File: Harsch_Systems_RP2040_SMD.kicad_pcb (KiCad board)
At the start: 2 copper layers, 140 parts, among them J1 Jack-DC, J2 USB_A, J3 DEBUG, J4 Conn_01x08_Female, J5 Conn_01x08_Female, J6 Conn_01x04_Female, J7 Conn_01x06_Female, Q1 BSS123, Q2 BSS123, Q3 BSS123, Q4 BSS123, Q5 BCP56, Q6 BCP56, Q7 BCP56, Q8 BCP56, SW1 SW_MEC_5E, U1 RP2040, U2 W25Q32JVSSIQ_TR, U3 LM324, U4 PC847, U5 LM324, U6 PC847, U7 PC847, U8 LM324, Y1 12MHz

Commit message: Finished the schematic, except for maybe a couple test points.
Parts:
- removed D1: D, Diode_SMD:D_0805_2012Metric
- added C35: 2.2μ, Capacitor_SMD:C_0805_2012Metric, F.Cu at (219.1, 135.9)
- added C36: 2.2μ, Capacitor_SMD:C_0805_2012Metric, F.Cu at (209.1, 121.2)
- added C37: 2.2μ, Capacitor_SMD:C_0805_2012Metric, F.Cu at (213.6, 118.2)
- added C38: 2.2μ, Capacitor_SMD:C_0805_2012Metric, F.Cu at (218.0, 112.1)
- added C39: 2.2μ, Capacitor_SMD:C_0805_2012Metric, F.Cu at (209.1, 118.2)
- added C40: 2.2μ, Capacitor_SMD:C_0805_2012Metric, F.Cu at (213.6, 115.2)
- added C41: 2.2μ, Capacitor_SMD:C_0805_2012Metric, F.Cu at (209.1, 115.2)
- added C42: 2.2μ, Capacitor_SMD:C_0805_2012Metric, F.Cu at (213.6, 112.1)
- added C43: 2.2μ, Capacitor_SMD:C_0805_2012Metric, F.Cu at (209.1, 112.1)
- added D3: D, Diode_SMD:D_0805_2012Metric, F.Cu at (238.2, 112.2)
- added D4: D, Diode_SMD:D_0805_2012Metric, F.Cu at (242.6, 112.2)
- added J8: DEBUG, Connector_PinHeader_2.54mm:PinHeader_1x03_P2.54mm_Vertical, F.Cu at (154.3, 55.9)
- added L1: 6.8μ, Inductor_SMD:L_Vishay_IHLP-2020, F.Cu at (204.9, 137.7)
- added R78: 10k, Resistor_SMD:R_0805_2012Metric, F.Cu at (209.1, 124.2)
- added R79: 22k, Resistor_SMD:R_0805_2012Metric, F.Cu at (222.4, 112.1)
- added R80: 22k, Resistor_SMD:R_0805_2012Metric, F.Cu at (218.0, 115.1)
- added U10: TLV9304IDR, Package_SO:SOIC-14_3.9x8.7mm_P1.27mm, F.Cu at (119.4, 134.5)
- added U9: ELQ3H7, Package_SO:SOP-16_3.9x9.9mm_P1.27mm, F.Cu at (165.2, 92.7)
- C1, C5: value 0.1μ -> 1μ; footprint Capacitor_SMD:C_0603_1608Metric -> Capacitor_SMD:C_0805_2012Metric
- C10, C11: value 1μ -> 0.1μ; footprint Capacitor_SMD:C_0805_2012Metric -> Capacitor_SMD:C_0603_1608Metric
- C12: value 27p -> 22μ
- C14: value 27p -> 0.1μ; footprint Capacitor_SMD:C_0805_2012Metric -> Capacitor_SMD:C_0603_1608Metric
- C15: value .47μ -> 0.1μ; footprint Capacitor_SMD:C_0805_2012Metric -> Capacitor_SMD:C_0603_1608Metric
- C16: value .47μ -> 22μ
- C17, C18: value 2.2µ -> 0.1μ; footprint Capacitor_SMD:C_0805_2012Metric -> Capacitor_SMD:C_0603_1608Metric
- C19, C20: value 2.2μ -> 1μ
- C21, C23: value 2.2μ -> 27p
- C22: value 2.2μ -> 0.1μ; footprint Capacitor_SMD:C_0805_2012Metric -> Capacitor_SMD:C_0603_1608Metric
- C24, C25: value 2.2μ -> .47μ
- C26, C27: value 2.2μ -> 2.2µ
- C3, C8: value 0.1μ -> 33n; footprint Capacitor_SMD:C_0603_1608Metric -> Capacitor_SMD:C_0805_2012Metric
- C4: value 0.1μ -> 10μ; footprint Capacitor_SMD:C_0603_1608Metric -> Capacitor_SMD:C_0805_2012Metric
- D2: value D -> D_Schottky; footprint Diode_SMD:D_0805_2012Metric -> Diode_SMD:D_SOD-123
- J2: value USB_A -> Conn_01x02_Male; footprint Connector_USB:USB_Micro-B_GCT_USB3076-30-A -> Connector_PinSocket_2.54mm:PinSocket_1x02_P2.54mm_Vertical
- J3: value DEBUG -> Conn_01x08_Female; footprint Connector_PinHeader_2.54mm:PinHeader_1x03_P2.54mm_Vertical -> Connector_PinHeader_2.54mm:PinHeader_1x08_P2.54mm_Vertical
- J5: value Conn_01x08_Female -> Conn_01x04_Female; footprint Connector_PinHeader_2.54mm:PinHeader_1x08_P2.54mm_Vertical -> Connector_PinHeader_2.54mm:PinHeader_1x04_P2.54mm_Vertical
- J6: value Conn_01x04_Female -> Conn_01x06_Female; footprint Connector_PinHeader_2.54mm:PinHeader_1x04_P2.54mm_Vertical -> Connector_PinHeader_2.54mm:PinHeader_1x06_P2.54mm_Vertical
- J7: value Conn_01x06_Female -> USB_A; footprint Connector_PinHeader_2.54mm:PinHeader_1x06_P2.54mm_Vertical -> Connector_USB:USB_Micro-B_GCT_USB3076-30-A
- Q5, Q6, Q7, Q8: footprint Package_TO_SOT_SMD:SOT-223-3_TabPin2 -> Package_TO_SOT_SMD:SOT-223
- R1, R2: value 27 -> 10K
- R10: value 10k -> 1K
- R11: value 10k -> 22k
- R12, R71, R72: value 2.2k -> 22k
- R13, R70: value 2.2k -> 10k
- R14: value 150 -> 10k
- R15: value 1M -> 2.2k
- R16, R30, R31, R38, R39: value 150 -> 2.2k
- R17: value 1M -> 150
- R18, R20: value 47 -> 1M; footprint Resistor_SMD:R_1210_3225Metric -> Resistor_SMD:R_0805_2012Metric
- R19: value 47 -> 150; footprint Resistor_SMD:R_1210_3225Metric -> Resistor_SMD:R_0805_2012Metric
- R22, R23: value 150 -> 47; footprint Resistor_SMD:R_0805_2012Metric -> Resistor_SMD:R_1210_3225Metric
- R24: value 2.2k -> 47; footprint Resistor_SMD:R_0805_2012Metric -> Resistor_SMD:R_1210_3225Metric
- R25, R26, R34: value 2.2k -> 150
- R3: value 10K -> 10k
- R32, R40: value 10 -> 2.2k
- R33, R41: value 10 -> 150
- R35, R36: value 2.2k -> 10
- R4: value 1K -> 53.6k
- R42: value 2.2k -> 150; footprint Resistor_SMD:R_1210_3225Metric -> Resistor_SMD:R_0805_2012Metric
- R43: value 2.2k -> 10; footprint Resistor_SMD:R_1210_3225Metric -> Resistor_SMD:R_0805_2012Metric
- R44: value 20k -> 10
- R45, R49: value 20k -> 2.2k; footprint Resistor_SMD:R_0805_2012Metric -> Resistor_SMD:R_1210_3225Metric
- R47: value 2.2k -> 20k; footprint Resistor_SMD:R_1210_3225Metric -> Resistor_SMD:R_0805_2012Metric
- R5: value 10K -> 1K
- R50: value 470 -> 2.2k; footprint Resistor_SMD:R_0805_2012Metric -> Resistor_SMD:R_1210_3225Metric
- R51: value 470 -> 20k
- R52: value 2.2k -> 20k
- R53, R59: value 4.7k -> 470
- R54, R60: value 2.2k -> 470
- R55, R61: value 4.7k -> 2.2k
- R56: value 470 -> 4.7k
- R57: value 470 -> 2.2k
- R58, R62, R64: value 2.2k -> 4.7k
- R6: value R_US -> 10K
- R66, R67, R74, R75: value 10k -> 2.2k
- R68, R76: value 22k -> 2.2k
- R69, R77: value 22k -> 10k
- R7: value 1K -> DNP
- R8, R9: value 22k -> 27
- SW1: footprint Button_Switch_SMD:Panasonic_EVQPUJ_EVQPUA -> Button_Switch_SMD:SW_DIP_SPSTx02_Slide_6.7x6.64mm_W6.73mm_P2.54mm_LowProfile_JPin
- U1: value RP2040 -> XC6210B332MR; footprint MCU_RaspberryPi_and_Boards:RP2040-QFN-56 -> Package_TO_SOT_SMD:SOT-23-5
- U2: value W25Q32JVSSIQ_TR -> TPS62933; footprint digikey-footprints:SOIC-8_W5.6mm -> Package_DFN_QFN:Texas_VSON-HR-8_1.5x2mm_P0.5mm
- U3: value LM324 -> RP2040; footprint Package_DIP:DIP-14_W7.62mm -> MCU_RaspberryPi_and_Boards:RP2040-QFN-56
- U4: value PC847 -> W25Q32JVSSIQ_TR; footprint Package_DIP:DIP-16_W7.62mm -> digikey-footprints:SOIC-8_W5.6mm
- U5: value LM324 -> TLV9004xRUCR; footprint Package_DIP:DIP-14_W7.62mm -> Package_SO:SOIC-14_3.9x8.7mm_P1.27mm
- U6: value PC847 -> ELQ3H7; footprint Package_DIP:DIP-16_W7.62mm -> Package_SO:SOP-16_3.9x9.9mm_P1.27mm
- U7: value PC847 -> TLV9004xRUCR; footprint Package_DIP:DIP-16_W7.62mm -> Package_SO:SOIC-14_3.9x8.7mm_P1.27mm
- U8: value LM324 -> ELQ3H7; footprint Package_DIP:DIP-14_W7.62mm -> Package_SO:SOP-16_3.9x9.9mm_P1.27mm
- moved J5 96.7 mm to (184.8, 26.0)
- moved J4 95.0 mm to (175.3, 21.0), turned to 270 degrees
- moved J6 88.2 mm to (184.8, 39.4)
- moved J3 82.0 mm to (150.5, 21.0), turned to 270 degrees
- moved SW1 68.4 mm to (172.1, 31.1)
- moved U3 66.0 mm to (154.9, 36.2)
- moved U8 62.4 mm to (141.0, 107.7)
- moved J7 43.8 mm to (124.5, 32.4), turned to 90 degrees
- moved J1 24.5 mm to (128.3, 50.8)
- moved U6 22.9 mm to (141.0, 92.7)
- moved U5 20.4 mm to (119.4, 121.3)
- moved U7 19.1 mm to (140.5, 121.3)
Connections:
- C1 pad 1: +1V1 -> +5V
- C10 pad 1: +1V1 -> +3V3
- C12 pad 1: /XIN -> +5V
- C14 pad 1: Net-(C14-Pad1) -> +5V
- C15 pad 1: /10V Input/ADC0 -> +3V3
- C16 pad 1: /10V Input/ADC1 -> +5V
- C17 pad 1: /20mA Input/ADC2 -> +3V3
- C18 pad 1: /20mA Input/ADC3 -> +3V3
- C19 pad 1: Net-(C19-Pad1) -> +1V1
- C2 pad 1: +1V1 -> +24V
- C20 pad 1: Net-(C20-Pad1) -> +3V3
- C21 pad 1: Net-(C21-Pad1) -> /XIN
- C22 pad 1: Net-(C22-Pad1) -> +3V3
- C24 pad 1: Net-(C24-Pad1) -> /ADC0
- C25 pad 1: Net-(C25-Pad1) -> /ADC1
- C26 pad 1: Net-(C26-Pad1) -> /ADC2
- C27 pad 1: Net-(C27-Pad1) -> /ADC3
- C3 pad 1: +3V3 -> Net-(C3-Pad1)
- C4 pad 1: +3V3 -> +24V
- C6 pad 1: +3V3 -> +1V1
- C7 pad 1: +3V3 -> +1V1
- C8 pad 1: +3V3 -> Net-(C8-Pad1)
- C8 pad 2: GND -> Net-(C8-Pad2)
- D2 pad 1: /Digital Input/IN+1 -> +24V
- J1 pad 1: Net-(J1-Pad1) -> Net-(D2-Pad2)
- J1 pad 2: Net-(J1-Pad2) -> GND
- J2 pad 1: Net-(J2-Pad1) -> GND
- J3 pad 1: /SWCLK -> /10V Output/OUT0
- J3 pad 2: GND -> /10V Output/OUT1
- J3 pad 3: /SWDIO -> /10V Output/OUT2
- J4 pad 1: Net-(J4-Pad1) -> /Digital Input/IN+0
- J4 pad 2: Net-(J4-Pad2) -> /Digital Input/IN-0
- J4 pad 3: Net-(J4-Pad3) -> /Digital Input/IN+1
- J4 pad 4: Net-(J4-Pad4) -> /Digital Input/IN-1
- J4 pad 5: Net-(J4-Pad5) -> /Digital Input/IN+2
- J4 pad 6: Net-(J4-Pad6) -> /Digital Input/IN-2
- J4 pad 7: Net-(J4-Pad7) -> /Digital Input/IN+3
- J4 pad 8: Net-(J4-Pad8) -> /Digital Input/IN-3
- J5 pad 1: Net-(J5-Pad1) -> /Digital Output/OUT0
- J5 pad 2: Net-(J5-Pad2) -> /Digital Output/OUT1
- J5 pad 3: Net-(J5-Pad3) -> /Digital Output/OUT2
- J5 pad 4: Net-(J5-Pad4) -> /Digital Output/OUT3
- J6 pad 1: Net-(J6-Pad1) -> /10V Input/VIN0
- J6 pad 2: Net-(J6-Pad2) -> /10V Input/VIN1
- J6 pad 3: Net-(J6-Pad3) -> /20mA Input/IN2
- J6 pad 4: Net-(J6-Pad4) -> /20mA Input/OUT2
- J7 pad 4: Net-(J7-Pad4) -> GND
- J7 pad 5: Net-(J7-Pad5) -> GND
- J7 pad 6: Net-(J7-Pad6) -> (no net)
- R1 pad 1: /USB_DP -> Net-(R1-Pad1)
- R1 pad 2: Net-(J2-Pad3) -> +5V
- R10 pad 1: GND -> /XOUT
- R10 pad 2: Net-(R10-Pad2) -> Net-(C23-Pad1)
- R11 pad 1: GND -> Net-(R11-Pad1)
- R11 pad 2: Net-(R11-Pad2) -> /10V Input/VIN0
- R12 pad 1: /10V Input/ADC0 -> Net-(R12-Pad1)
- R12 pad 2: Net-(R12-Pad2) -> /10V Input/VIN1
- R13 pad 1: /10V Input/ADC1 -> GND
- R13 pad 2: Net-(R13-Pad2) -> Net-(R11-Pad1)
- R14 pad 1: Net-(R14-Pad1) -> GND
- R14 pad 2: /20mA Input/IN2 -> Net-(R12-Pad1)
- R15 pad 1: GND -> /ADC0
- R15 pad 2: /20mA Input/OUT2 -> Net-(R15-Pad2)
- R16 pad 1: Net-(R16-Pad1) -> /ADC1
- R16 pad 2: /20mA Input/IN3 -> Net-(R16-Pad2)
- R17 pad 1: GND -> Net-(R17-Pad1)
- R17 pad 2: /20mA Input/OUT3 -> /20mA Input/IN2
- R18 pad 2: Net-(R18-Pad2) -> /20mA Input/OUT2
- R19 pad 1: GND -> Net-(R19-Pad1)
- R19 pad 2: Net-(R19-Pad2) -> /20mA Input/IN3
- R2 pad 1: /USB_DM -> Net-(R2-Pad1)
- R2 pad 2: Net-(J2-Pad2) -> +3V3
- R20 pad 2: Net-(R20-Pad2) -> /20mA Input/OUT3
- R24 pad 1: /20mA Input/ADC2 -> GND
- R24 pad 2: Net-(R22-Pad2) -> Net-(R24-Pad2)
- R25 pad 1: /20mA Input/ADC3 -> GND
- R25 pad 2: Net-(R23-Pad2) -> Net-(R25-Pad2)
- R26 pad 1: Net-(C19-Pad1) -> GND
- R26 pad 2: /20mA Output/PWM4 -> Net-(R26-Pad2)
- R27 pad 1: Net-(C20-Pad1) -> /ADC2
- R27 pad 2: /20mA Output/PWM5 -> Net-(R25-Pad2)
- R28 pad 1: Net-(C21-Pad1) -> /ADC3
- R28 pad 2: Net-(C19-Pad1) -> Net-(R26-Pad2)
- R29 pad 1: Net-(C22-Pad1) -> Net-(C28-Pad1)
- R29 pad 2: Net-(C20-Pad1) -> /PWM4
- R3 pad 1: Net-(R3-Pad1) -> GND
- R3 pad 2: +3V3 -> Net-(R3-Pad2)
- R30 pad 1: Net-(Q1-Pad2) -> Net-(C29-Pad1)
- R30 pad 2: GND -> /PWM5
- R31 pad 1: Net-(Q2-Pad2) -> Net-(C30-Pad1)
- R31 pad 2: GND -> Net-(C28-Pad1)
- R32 pad 1: Net-(Q1-Pad1) -> Net-(C31-Pad1)
- R32 pad 2: Net-(R32-Pad2) -> Net-(C29-Pad1)
- R33 pad 1: Net-(Q2-Pad1) -> Net-(Q1-Pad2)
- R33 pad 2: Net-(R33-Pad2) -> GND
- R34 pad 1: Net-(C23-Pad1) -> Net-(Q2-Pad2)
- R34 pad 2: /20mA Output/PWM6 -> GND
- R35 pad 1: Net-(C24-Pad1) -> Net-(Q1-Pad1)
- R35 pad 2: /20mA Output/PWM7 -> Net-(R35-Pad2)
- R36 pad 1: Net-(C25-Pad1) -> Net-(Q2-Pad1)
- R36 pad 2: Net-(C23-Pad1) -> Net-(R36-Pad2)
- R37 pad 1: Net-(C26-Pad1) -> Net-(C32-Pad1)
- R37 pad 2: Net-(C24-Pad1) -> /PWM6
- R38 pad 1: Net-(Q3-Pad2) -> Net-(C33-Pad1)
- R38 pad 2: GND -> /PWM7
- R39 pad 1: Net-(Q4-Pad2) -> Net-(C34-Pad1)
- R39 pad 2: GND -> Net-(C32-Pad1)
- R4 pad 1: /QSPI_CS -> Net-(R3-Pad2)
- R4 pad 2: /USB_BOOT -> +5V
- R40 pad 1: Net-(Q3-Pad1) -> Net-(C35-Pad1)
- R40 pad 2: Net-(R40-Pad2) -> Net-(C33-Pad1)
- R41 pad 1: Net-(Q4-Pad1) -> Net-(Q3-Pad2)
- R41 pad 2: Net-(R41-Pad2) -> GND
- R42 pad 1: /Digital Input/IN-0 -> Net-(Q4-Pad2)
- R42 pad 2: Net-(D1-Pad2) -> GND
- R43 pad 1: /Digital Input/IN-1 -> Net-(Q3-Pad1)
- R43 pad 2: Net-(D2-Pad2) -> Net-(R43-Pad2)
- R44 pad 1: 3.3V -> Net-(Q4-Pad1)
- R44 pad 2: /Digital Input/GPIO0 -> Net-(R44-Pad2)
- R45 pad 1: 3.3V -> /Digital Input/IN-0
- R45 pad 2: /Digital Input/GPIO1 -> Net-(D3-Pad2)
- R46 pad 1: /Digital Input/IN-2 -> /Digital Input/IN-1
- R46 pad 2: Net-(D5-Pad2) -> Net-(D4-Pad2)
- R47 pad 1: /Digital Input/IN-3 -> 3.3V
- R47 pad 2: Net-(D6-Pad2) -> /GPIO1
- R48 pad 2: /Digital Input/GPIO2 -> /GPIO3
- R49 pad 1: 3.3V -> /Digital Input/IN-2
- R49 pad 2: /Digital Input/GPIO3 -> Net-(D5-Pad2)
- R5 pad 1: +3V3 -> /QSPI_CS
- R5 pad 2: /QSPI_CS -> Net-(R5-Pad2)
- R50 pad 1: GND -> /Digital Input/IN-3
- R50 pad 2: Net-(R50-Pad2) -> Net-(D6-Pad2)
- R51 pad 1: GND -> 3.3V
- R51 pad 2: Net-(R51-Pad2) -> /GPIO5
- R52 pad 1: Net-(R52-Pad1) -> 3.3V
- R52 pad 2: Net-(Q5-Pad1) -> /GPIO7
- R53 pad 2: /Digital Output/OUT0 -> Net-(R53-Pad2)
- R54 pad 1: Net-(R54-Pad1) -> GND
- R54 pad 2: Net-(Q6-Pad1) -> Net-(R54-Pad2)
- R55 pad 1: GND -> Net-(R55-Pad1)
- R55 pad 2: /Digital Output/OUT1 -> Net-(Q5-Pad1)
- R56 pad 2: Net-(R56-Pad2) -> /Digital Output/OUT0
- R57 pad 1: GND -> Net-(R57-Pad1)
- R57 pad 2: Net-(R57-Pad2) -> Net-(Q6-Pad1)
- R58 pad 1: Net-(R58-Pad1) -> GND
- R58 pad 2: Net-(Q7-Pad1) -> /Digital Output/OUT1
- R59 pad 2: /Digital Output/OUT2 -> Net-(R59-Pad2)
- R6 pad 1: /XIN -> +3V3
- R6 pad 2: /XOUT -> /QSPI_CS
- R60 pad 1: Net-(R60-Pad1) -> GND
- R60 pad 2: Net-(Q8-Pad1) -> Net-(R60-Pad2)
- R61 pad 1: GND -> Net-(R61-Pad1)
- R61 pad 2: /Digital Output/OUT3 -> Net-(Q7-Pad1)
- R62 pad 1: Net-(C27-Pad1) -> GND
- R62 pad 2: /10V Output/PWM0 -> /Digital Output/OUT2
- R63 pad 1: Net-(C28-Pad1) -> Net-(R63-Pad1)
- R63 pad 2: /10V Output/PWM1 -> Net-(Q8-Pad1)
- R64 pad 1: Net-(C29-Pad1) -> GND
- R64 pad 2: Net-(C27-Pad1) -> /Digital Output/OUT3
- R65 pad 1: Net-(C30-Pad1) -> Net-(C36-Pad1)
- R65 pad 2: Net-(C28-Pad1) -> /PWM0
- R66 pad 1: Net-(R66-Pad1) -> Net-(C37-Pad1)
- R66 pad 2: GND -> /PWM1
- R67 pad 1: Net-(R67-Pad1) -> Net-(C38-Pad1)
- R67 pad 2: GND -> Net-(C36-Pad1)
- R68 pad 1: /10V Output/OUT0 -> Net-(C39-Pad1)
- R68 pad 2: Net-(R66-Pad1) -> Net-(C37-Pad1)
- R69 pad 1: /10V Output/OUT1 -> Net-(R69-Pad1)
- R69 pad 2: Net-(R67-Pad1) -> GND
- R7 pad 1: /XOUT -> /XIN
- R7 pad 2: Net-(C14-Pad1) -> /XOUT
- R70 pad 1: Net-(C31-Pad1) -> Net-(R70-Pad1)
- R70 pad 2: /10V Output/PWM2 -> GND
- R71 pad 1: Net-(C32-Pad1) -> /10V Output/OUT0
- R71 pad 2: /10V Output/PWM3 -> Net-(R69-Pad1)
- R72 pad 1: Net-(C33-Pad1) -> /10V Output/OUT1
- R72 pad 2: Net-(C31-Pad1) -> Net-(R70-Pad1)
- R73 pad 1: Net-(C34-Pad1) -> Net-(C40-Pad1)
- R73 pad 2: Net-(C32-Pad1) -> /PWM2
- R74 pad 1: Net-(R74-Pad1) -> Net-(C41-Pad1)
- R74 pad 2: GND -> /PWM3
- R75 pad 1: Net-(R75-Pad1) -> Net-(C42-Pad1)
- R75 pad 2: GND -> Net-(C40-Pad1)
- R76 pad 1: /10V Output/OUT2 -> Net-(C43-Pad1)
- R76 pad 2: Net-(R74-Pad1) -> Net-(C41-Pad1)
- R77 pad 1: /10V Output/OUT3 -> Net-(R77-Pad1)
- R77 pad 2: Net-(R75-Pad1) -> GND
- R8 pad 1: Net-(R10-Pad2) -> /USB_DP
- R8 pad 2: /10V Input/VIN0 -> Net-(J7-Pad3)
- R9 pad 1: Net-(R11-Pad2) -> /USB_DM
- R9 pad 2: /10V Input/VIN1 -> Net-(J7-Pad2)
- SW1 pad 1: /USB_BOOT -> Net-(R5-Pad2)
- SW1 pad 2: /USB_BOOT -> Net-(R5-Pad2)
- U1 pad 1: +3V3 -> +5V
- U1 pad 2: /10V Output/PWM0 -> GND
- U1 pad 3: /Digital Input/GPIO0 -> Net-(R1-Pad1)
- U1 pad 4: /10V Output/PWM1 -> Net-(U1-Pad4)
- U1 pad 5: /Digital Input/GPIO1 -> +3V3
- U2 pad 1: /QSPI_CS -> Net-(J2-Pad2)
- U2 pad 2: /QSPI_SD0 -> Net-(U2-Pad2)
- U2 pad 3: /QSPI_SD2 -> +24V
- U2 pad 5: /QSPI_SD1 -> Net-(C8-Pad2)
- U2 pad 6: /QSPI_SCK -> Net-(C8-Pad1)
- U2 pad 7: /QSPI_SD3 -> Net-(C3-Pad1)
- U2 pad 8: +3V3 -> Net-(R3-Pad2)
- U3 pad 1: Net-(R12-Pad2) -> +3V3
- U3 pad 10: Net-(R18-Pad2) -> +3V3
- U3 pad 11: Net-(U3-Pad11) -> /PWM4
- U3 pad 12: Net-(R19-Pad2) -> /GPIO9
- U3 pad 13: Net-(R21-Pad2) -> /PWM5
- U3 pad 14: Net-(U3-Pad14) -> /GPIO11
- U3 pad 2: Net-(R12-Pad2) -> /PWM0
- U3 pad 3: Net-(R10-Pad2) -> /GPIO1
- U3 pad 4: Net-(U3-Pad4) -> /PWM1
- U3 pad 5: Net-(R11-Pad2) -> /GPIO3
- U3 pad 6: Net-(R13-Pad2) -> /PWM2
- U3 pad 7: Net-(R13-Pad2) -> /GPIO5
- U3 pad 8: Net-(U3-Pad8) -> /PWM3
- U3 pad 9: Net-(R20-Pad2) -> /GPIO7
- U4 pad 1: Net-(R14-Pad1) -> /QSPI_CS
- U4 pad 2: /20mA Input/OUT2 -> /QSPI_SD0
- U4 pad 3: Net-(R16-Pad1) -> /QSPI_SD2
- U4 pad 4: /20mA Input/OUT3 -> GND
- U4 pad 5: Net-(U3-Pad8) -> /QSPI_SD1
- U4 pad 6: Net-(R22-Pad2) -> /QSPI_SCK
- U4 pad 7: Net-(U3-Pad14) -> /QSPI_SD3
- U4 pad 8: Net-(R23-Pad2) -> +3V3
- U5 pad 1: Net-(R32-Pad2) -> Net-(R15-Pad2)
- U5 pad 10: Net-(C25-Pad1) -> GND
- U5 pad 11: GND -> Net-(R22-Pad2)
- U5 pad 12: Net-(C26-Pad1) -> Net-(R24-Pad2)
- U5 pad 13: Net-(Q4-Pad2) -> Net-(U5-Pad13)
- U5 pad 14: Net-(R41-Pad2) -> Net-(R15-Pad2)
- U5 pad 2: Net-(Q1-Pad2) -> Net-(R11-Pad1)
- U5 pad 3: Net-(C21-Pad1) -> +5V
- U5 pad 4: +10V -> Net-(R12-Pad1)
- U5 pad 5: Net-(C22-Pad1) -> Net-(R16-Pad2)
- U5 pad 6: Net-(Q2-Pad2) -> Net-(R16-Pad2)
- U5 pad 7: Net-(R33-Pad2) -> Net-(U5-Pad7)
- U5 pad 8: Net-(R40-Pad2) -> Net-(R23-Pad2)
- U5 pad 9: Net-(Q3-Pad2) -> Net-(R21-Pad2)
- U6 pad 1: /Digital Input/IN+0 -> Net-(R17-Pad1)
- U6 pad 10: /Digital Input/GPIO3 -> Net-(U5-Pad13)
- U6 pad 11: GND -> Net-(R25-Pad2)
- U6 pad 12: /Digital Input/GPIO2 -> Net-(U5-Pad7)
- U6 pad 13: GND -> Net-(R22-Pad2)
- U6 pad 14: /Digital Input/GPIO1 -> 3.3V
- U6 pad 15: GND -> Net-(R21-Pad2)
- U6 pad 16: /Digital Input/GPIO0 -> 3.3V
- U6 pad 2: Net-(D1-Pad2) -> /20mA Input/OUT2
- U6 pad 3: /Digital Input/IN+1 -> Net-(R19-Pad1)
- U6 pad 4: Net-(D2-Pad2) -> /20mA Input/OUT3
- U6 pad 5: /Digital Input/IN+2 -> 3.3V
- U6 pad 6: Net-(D5-Pad2) -> Net-(R23-Pad2)
- U6 pad 7: /Digital Input/IN+3 -> 3.3V
- U6 pad 8: Net-(D6-Pad2) -> Net-(R24-Pad2)
- U6 pad 9: GND -> Net-(R26-Pad2)
- U7 pad 1: /Digital Output/GPIO4 -> Net-(Q1-Pad2)
- U7 pad 10: 24V -> GND
- U7 pad 11: Net-(R58-Pad1) -> Net-(C35-Pad1)
- U7 pad 12: 24V -> Net-(Q4-Pad2)
- U7 pad 13: Net-(R54-Pad1) -> Net-(R44-Pad2)
- U7 pad 14: 24V -> Net-(R35-Pad2)
- U7 pad 2: Net-(R50-Pad2) -> Net-(C30-Pad1)
- U7 pad 3: /Digital Output/GPIO5 -> +5V
- U7 pad 4: Net-(R51-Pad2) -> Net-(C31-Pad1)
- U7 pad 5: /Digital Output/GPIO6 -> Net-(Q2-Pad2)
- U7 pad 6: Net-(R56-Pad2) -> Net-(R36-Pad2)
- U7 pad 7: /Digital Output/GPIO7 -> Net-(R43-Pad2)
- U7 pad 8: Net-(R57-Pad2) -> Net-(Q3-Pad2)
- U7 pad 9: Net-(R60-Pad1) -> Net-(C34-Pad1)
- U8 pad 1: /10V Output/OUT0 -> /Digital Input/IN+0
- U8 pad 10: Net-(C33-Pad1) -> /GPIO7
- U8 pad 12: Net-(C34-Pad1) -> /GPIO5
- U8 pad 13: Net-(R75-Pad1) -> GND
- U8 pad 14: /10V Output/OUT3 -> /GPIO3
- U8 pad 2: Net-(R66-Pad1) -> Net-(D3-Pad2)
- U8 pad 3: Net-(C29-Pad1) -> /Digital Input/IN+1
- U8 pad 4: +24V -> Net-(D4-Pad2)
- U8 pad 5: Net-(C30-Pad1) -> /Digital Input/IN+2
- U8 pad 6: Net-(R67-Pad1) -> Net-(D5-Pad2)
- U8 pad 7: /10V Output/OUT1 -> /Digital Input/IN+3
- U8 pad 8: /10V Output/OUT2 -> Net-(D6-Pad2)
- U8 pad 9: Net-(R74-Pad1) -> GND
- Y1 pad 2: Net-(C14-Pad1) -> Net-(C23-Pad1)

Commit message: Starting routing
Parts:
- added D1: LED, LED_SMD:LED_0805_2012Metric, F.Cu at (111.8, 66.7)
- added R81: 470, Resistor_SMD:R_0805_2012Metric, F.Cu at (111.7, 69.7)
- added TP1: TestPoint, Connector_PinSocket_2.54mm:PinSocket_1x01_P2.54mm_Vertical, F.Cu at (102.6, 67.5)
- added TP2: TestPoint, Connector_PinSocket_2.54mm:PinSocket_1x01_P2.54mm_Vertical, F.Cu at (102.6, 72.1)
- added TP3: TestPoint, Connector_PinSocket_2.54mm:PinSocket_1x01_P2.54mm_Vertical, F.Cu at (107.2, 67.5)
- added TP4: TestPoint, Connector_PinSocket_2.54mm:PinSocket_1x01_P2.54mm_Vertical, F.Cu at (107.2, 72.1)
- C10, C11, C13, C15, C17, C6, C7, C9: footprint Capacitor_SMD:C_0603_1608Metric -> Capacitor_SMD:C_0402_1005Metric_Pad0.74x0.62mm_HandSolder
- SW1: footprint Button_Switch_SMD:SW_DIP_SPSTx02_Slide_6.7x6.64mm_W6.73mm_P2.54mm_LowProfile_JPin -> Button_Switch_SMD:SW_SPST_Omron_B3FS-100xP
- moved C17 80.9 mm to (153.4, 29.7)
- moved C11 64.1 mm to (132.3, 31.0), turned to 90 degrees
- moved C6 61.7 mm to (130.2, 31.0), turned to 90 degrees
- moved C10 61.4 mm to (135.6, 33.5)
- moved C13 56.1 mm to (131.3, 31.0), turned to 90 degrees
- moved C7 54.8 mm to (134.0, 31.8), turned to 90 degrees
- moved C9 51.6 mm to (135.6, 32.4)
- moved J2 41.4 mm to (107.3, 41.3)
- moved U3 23.6 mm to (131.4, 38.2)
- moved J1 19.8 mm to (108.6, 52.7)
- moved J7 19.0 mm to (105.4, 32.4)
- moved J3 11.9 mm to (139.1, 17.8)
- moved J4 10.0 mm to (165.7, 17.8)
- moved SW1 6.54 mm to (175.3, 25.4)
- moved J8 5.12 mm to (149.2, 56.5)
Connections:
- U3 pad 23: +3V3 -> +1V1
- U3 pad 37: Net-(U3-Pad37) -> /GPIO25
- U3 pad 50: +3V3 -> +1V1
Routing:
- net +3V3: track 0.00 -> 11.1 mm
- net +1V1: track 0.00 -> 6.28 mm
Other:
- net class 10V O added: clearance 0.3, trace_width 0.4, via_dia 0.8, via_drill 0.4
- net class 24V added: clearance 0.4, trace_width 0.8, via_dia 1, via_drill 0.5
- net class 3.3V added: clearance 0.2, trace_width 0.2, via_dia 0.8, via_drill 0.4
- net class 5V added: clearance 0.4, trace_width 0.5, via_dia 0.8, via_drill 0.4
- net class Default: trace_width 0.25 -> 0.2
- net class GND added: clearance 0.2, trace_width 0.2, via_dia 0.8, via_drill 0.4
- net class MID SIGNAL added: clearance 0.25, trace_width 0.25, via_dia 0.8, via_drill 0.4
- net class SMALL SIGNAL added: clearance 0.2, trace_width 0.2, via_dia 0.8, via_drill 0.4

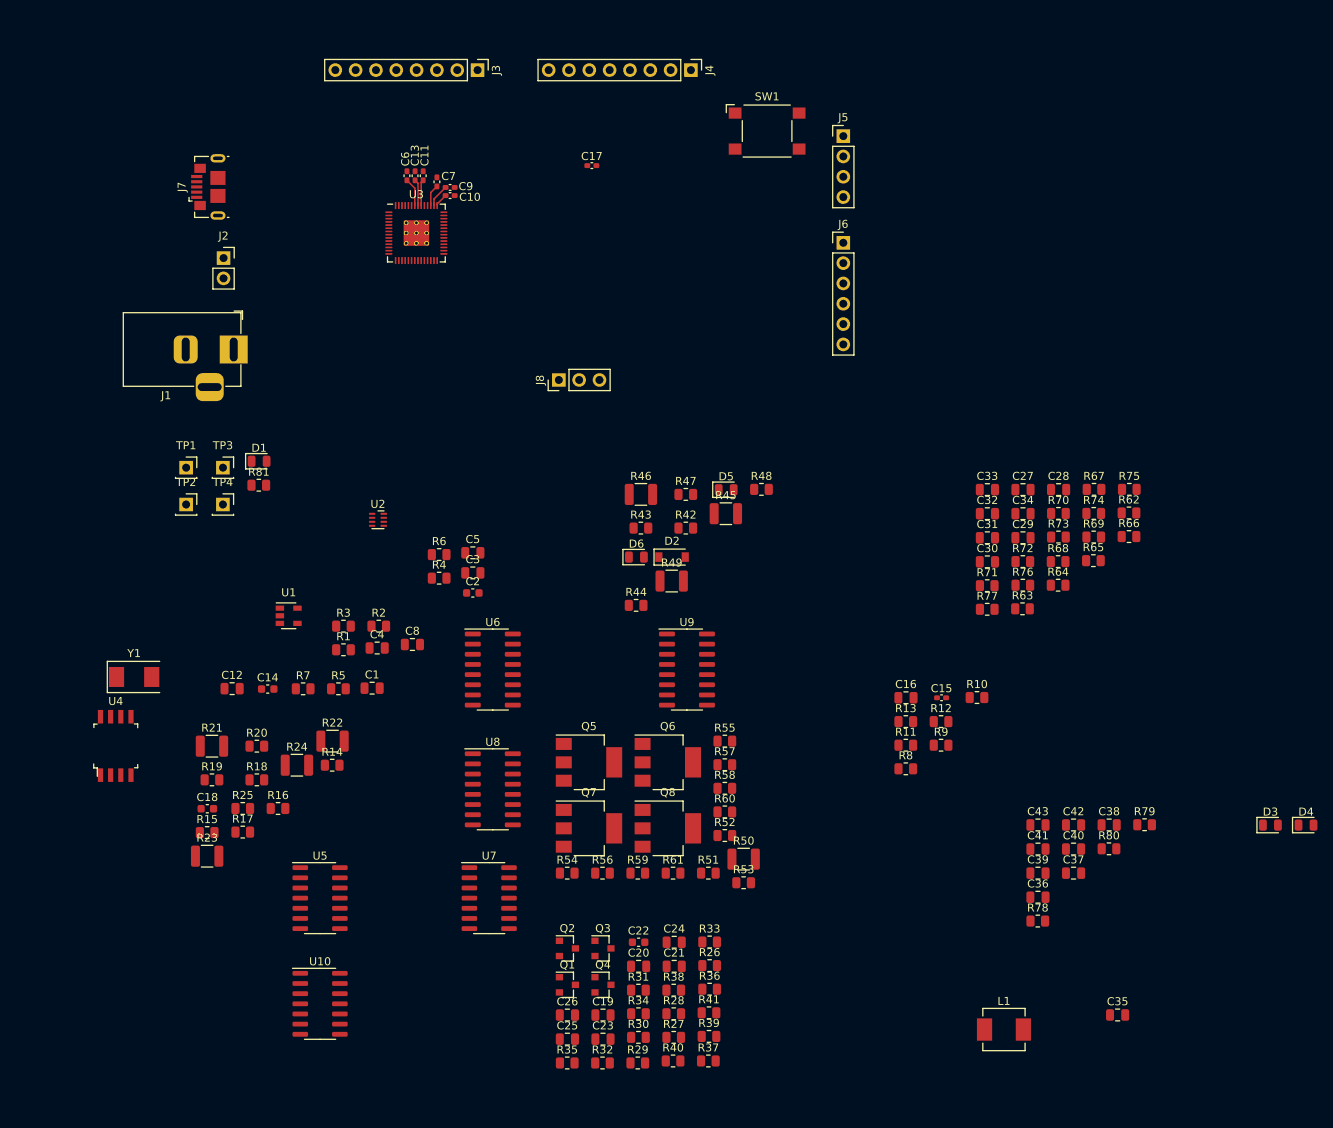
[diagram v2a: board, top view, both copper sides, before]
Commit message: Routing for all analog outputs
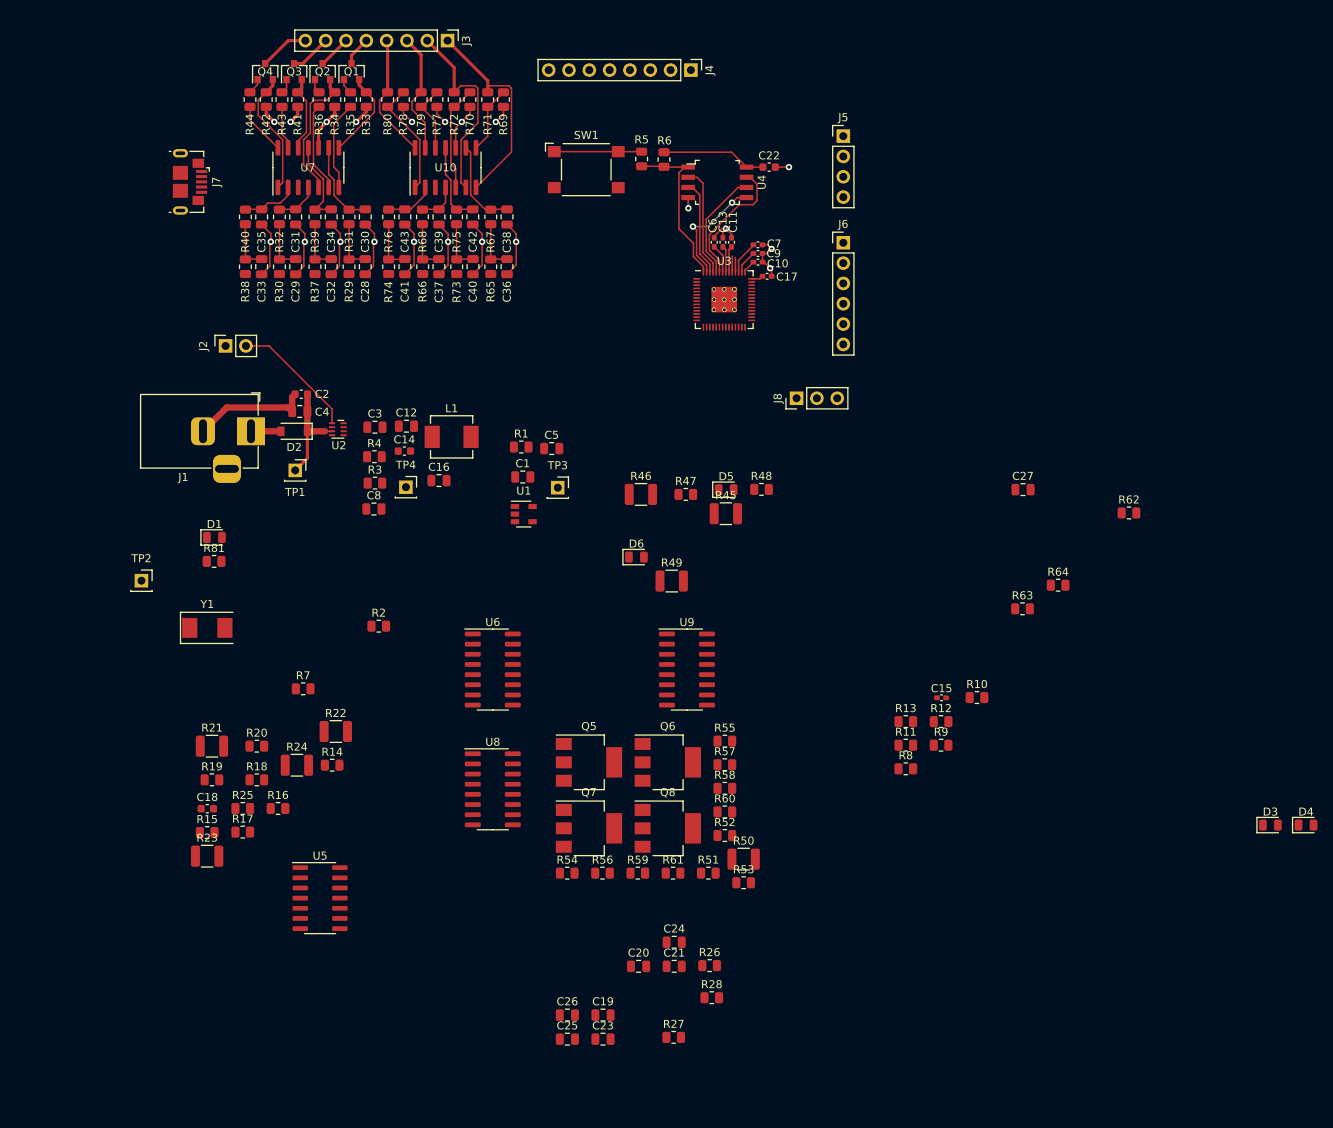
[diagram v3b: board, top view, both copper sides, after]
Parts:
- moved C35 146.3 mm to (112.1, 36.1), turned to 270 degrees
- moved R80 130.0 mm to (127.8, 21.5), turned to 270 degrees
- moved R78 129.7 mm to (129.8, 21.5), turned to 270 degrees
- moved R79 128.0 mm to (132.0, 21.5), turned to 270 degrees
- moved R41 125.2 mm to (116.6, 21.5), turned to 270 degrees
- moved R35 123.4 mm to (123.2, 21.5), turned to 270 degrees
- moved Q4 121.7 mm to (112.5, 18.0), turned to 90 degrees
- moved R36 121.5 mm to (119.3, 21.5), turned to 270 degrees
- moved R34 120.4 mm to (121.2, 21.5), turned to 270 degrees
- moved R40 118.3 mm to (110.0, 36.1), turned to 270 degrees
- moved Q1 117.3 mm to (123.3, 18.0), turned to 90 degrees
- moved Q3 116.2 mm to (116.1, 18.0), turned to 90 degrees
- moved Q2 113.8 mm to (119.7, 18.0), turned to 90 degrees
- moved R33 113.7 mm to (125.2, 21.5), turned to 270 degrees
- moved R39 113.7 mm to (118.7, 36.1), turned to 270 degrees
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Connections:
- U10 pad 1: Net-(R69-Pad1) -> Net-(R78-Pad1)
- U10 pad 11: Net-(C43-Pad1) -> Net-(C42-Pad1)
- U10 pad 12: Net-(R78-Pad1) -> Net-(R77-Pad1)
- U10 pad 13: /10V Output/OUT3 -> /10V Output/OUT2
- U10 pad 14: /10V Output/OUT0 -> /10V Output/OUT3
- U10 pad 2: Net-(C38-Pad1) -> Net-(C43-Pad1)
- U10 pad 7: /10V Output/OUT2 -> /10V Output/OUT0
- U10 pad 8: Net-(R77-Pad1) -> Net-(R69-Pad1)
- U10 pad 9: Net-(C42-Pad1) -> Net-(C38-Pad1)
- U7 pad 1: Net-(Q1-Pad2) -> Net-(Q4-Pad2)
- U7 pad 11: Net-(C35-Pad1) -> Net-(C34-Pad1)
- U7 pad 12: Net-(Q4-Pad2) -> Net-(Q3-Pad2)
- U7 pad 13: Net-(R44-Pad2) -> Net-(R43-Pad2)
- U7 pad 14: Net-(R35-Pad2) -> Net-(R44-Pad2)
- U7 pad 2: Net-(C30-Pad1) -> Net-(C35-Pad1)
- U7 pad 7: Net-(R43-Pad2) -> Net-(R35-Pad2)
- U7 pad 8: Net-(Q3-Pad2) -> Net-(Q1-Pad2)
- U7 pad 9: Net-(C34-Pad1) -> Net-(C30-Pad1)
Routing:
- net GND: track 0.00 -> 112.0 mm, vias 0 -> 21
- net /10V Output/OUT0: track 0.00 -> 26.5 mm
- net /10V Output/OUT1: track 0.00 -> 24.8 mm
- net /QSPI_CS: track 0.00 -> 21.0 mm
- net Net-(Q2-Pad2): track 0.00 -> 17.1 mm
- net /QSPI_SD3: track 0.00 -> 16.6 mm
- net Net-(J2-Pad2): track 0.00 -> 15.8 mm
- net Net-(Q4-Pad2): track 0.00 -> 15.7 mm
- net /10V Output/OUT3: track 0.00 -> 15.7 mm
- net /10V Output/OUT2: track 0.00 -> 15.3 mm
- net +3V3: track 11.1 -> 25.9 mm
- net Net-(R78-Pad1): track 0.00 -> 14.7 mm
- net /QSPI_SD1: track 0.00 -> 14.6 mm, vias 0 -> 2
- net /QSPI_SCK: track 0.00 -> 13.8 mm
- net /QSPI_SD0: track 0.00 -> 13.8 mm
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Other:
- net class 10V O: clearance 0.3 -> 0.2
- net class 5V: clearance 0.4 -> 0.2; trace_width 0.5 -> 0.4

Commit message: Routed ADC inputs and adjusted some trace widths
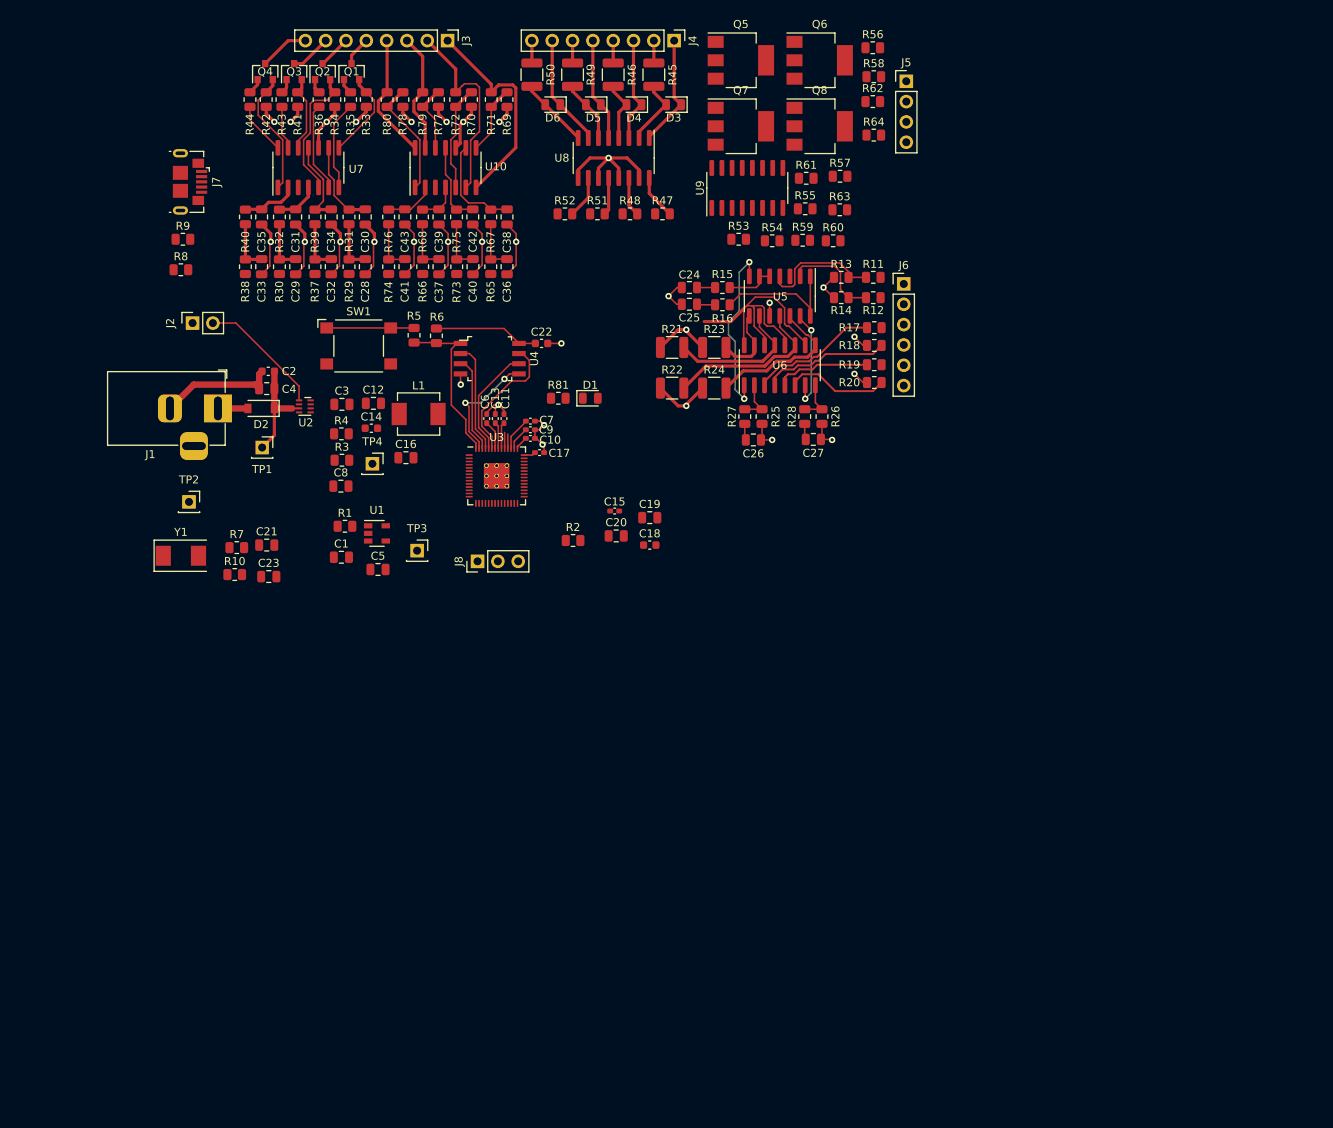
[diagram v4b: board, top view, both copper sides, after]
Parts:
- moved D4 123.2 mm to (158.6, 22.1), turned to 180 degrees
- moved D3 116.9 mm to (163.6, 22.1), turned to 180 degrees
- moved R9 113.9 mm to (102.2, 38.9)
- moved R8 110.0 mm to (102.0, 42.7)
- moved R56 108.6 mm to (188.5, 15.0)
- moved R50 101.6 mm to (145.9, 18.4), turned to 270 degrees
- moved R17 101.0 mm to (188.7, 50.0)
- moved R19 97.7 mm to (188.7, 54.6)
- moved U5 94.7 mm to (176.8, 46.0), turned to 270 degrees
- moved R18 94.4 mm to (188.7, 52.2)
- moved R10 94.0 mm to (108.7, 80.8)
- moved R15 93.8 mm to (169.7, 45.0)
- moved C25 93.1 mm to (165.5, 47.1), turned to 180 degrees
- moved R58 90.9 mm to (188.6, 18.6)
- moved R23 89.8 mm to (168.7, 52.5)
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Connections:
- U5 pad 1: Net-(R15-Pad2) -> Net-(R16-Pad2)
- U5 pad 14: Net-(R15-Pad2) -> Net-(R16-Pad2)
- U5 pad 2: Net-(R11-Pad1) -> Net-(R12-Pad1)
- U5 pad 4: Net-(R12-Pad1) -> Net-(R11-Pad1)
- U5 pad 5: Net-(R16-Pad2) -> Net-(R15-Pad2)
- U5 pad 6: Net-(R16-Pad2) -> Net-(R15-Pad2)
- U6 pad 1: Net-(R17-Pad1) -> Net-(U5-Pad7)
- U6 pad 10: Net-(U5-Pad13) -> 3.3V
- U6 pad 11: Net-(R25-Pad2) -> Net-(R22-Pad2)
- U6 pad 12: Net-(U5-Pad7) -> 3.3V
- U6 pad 13: Net-(R22-Pad2) -> Net-(R21-Pad2)
- U6 pad 15: Net-(R21-Pad2) -> Net-(R23-Pad2)
- U6 pad 2: /20mA Input/OUT2 -> Net-(R25-Pad2)
- U6 pad 3: Net-(R19-Pad1) -> Net-(R17-Pad1)
- U6 pad 4: /20mA Input/OUT3 -> /20mA Input/OUT2
- U6 pad 5: 3.3V -> Net-(R19-Pad1)
- U6 pad 6: Net-(R23-Pad2) -> /20mA Input/OUT3
- U6 pad 7: 3.3V -> Net-(U5-Pad13)
- U6 pad 8: Net-(R24-Pad2) -> Net-(R26-Pad2)
- U6 pad 9: Net-(R26-Pad2) -> Net-(R24-Pad2)
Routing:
- net GND: track 112.0 -> 165.1 mm, vias 21 -> 31
- net 3.3V: track 0.00 -> 37.0 mm
- net Net-(U5-Pad7): track 0.00 -> 22.4 mm, vias 0 -> 2
- net Net-(R22-Pad2): track 0.00 -> 20.9 mm
- net Net-(R24-Pad2): track 0.00 -> 19.2 mm
- net Net-(R21-Pad2): track 0.00 -> 17.7 mm
- net Net-(R16-Pad2): track 0.00 -> 17.6 mm
- net Net-(R17-Pad1): track 0.00 -> 16.1 mm
- net /20mA Input/OUT2: track 0.00 -> 16.0 mm
- net Net-(R11-Pad1): track 0.00 -> 15.4 mm
- net /Digital Input/IN+0: track 0.00 -> 14.2 mm
- net /Digital Input/IN+3: track 0.00 -> 14.0 mm
- net /Digital Input/IN+1: track 0.00 -> 13.2 mm
- net /Digital Input/IN+2: track 0.00 -> 13.0 mm
- net /20mA Input/OUT3: track 0.00 -> 13.0 mm
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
